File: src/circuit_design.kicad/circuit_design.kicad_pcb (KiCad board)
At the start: 2 copper layers, 220.3 x 182.9 mm, 184 parts, among them J1 CONN_BAT, Q1 BT136-600, Q2 BT136-600, Q3 BT136-600, Q4 BT136-600, U1 К176ИЕ12, U10 К155ЛА4, U11 К155ЛИ1, U12 К155ЛА1, U13 К155ИЕ5, U14 К155ЛЛ1, U15 К155ЛН1, U16 К155ЛИ1, U17 К155ТВ15, U18 К155ИЕ5, U19 К155ЛП5, U2 К155ЛП10, U20 К155ИВ1, U21 К155ИД7, U22 К155ИД4, U23 К155ЛН1, U24 К155ЛП10, U25 MOC3062M, U26 MOC3062M, U27 MOC3062M, U28 MOC3062M, U29 LM7806_TO220, U3 К155ЛЕ3, U30 SC6038, U31 К155ЛЕ1, U32 К155ЛН1, U33 К155ЛИ1, U34 К155ЛА4, U35 К155ТВ15, U36 К155ТЛ2, U37 4020, U38 LM7806_TO220, U39 К155ЛН1, U4 К155ЛН1, U5 К155ЛИ1, U6 К155ЛЛ1, U7 4020, U8 ICL7660, U9 К155ИЕ5, Y1 32768

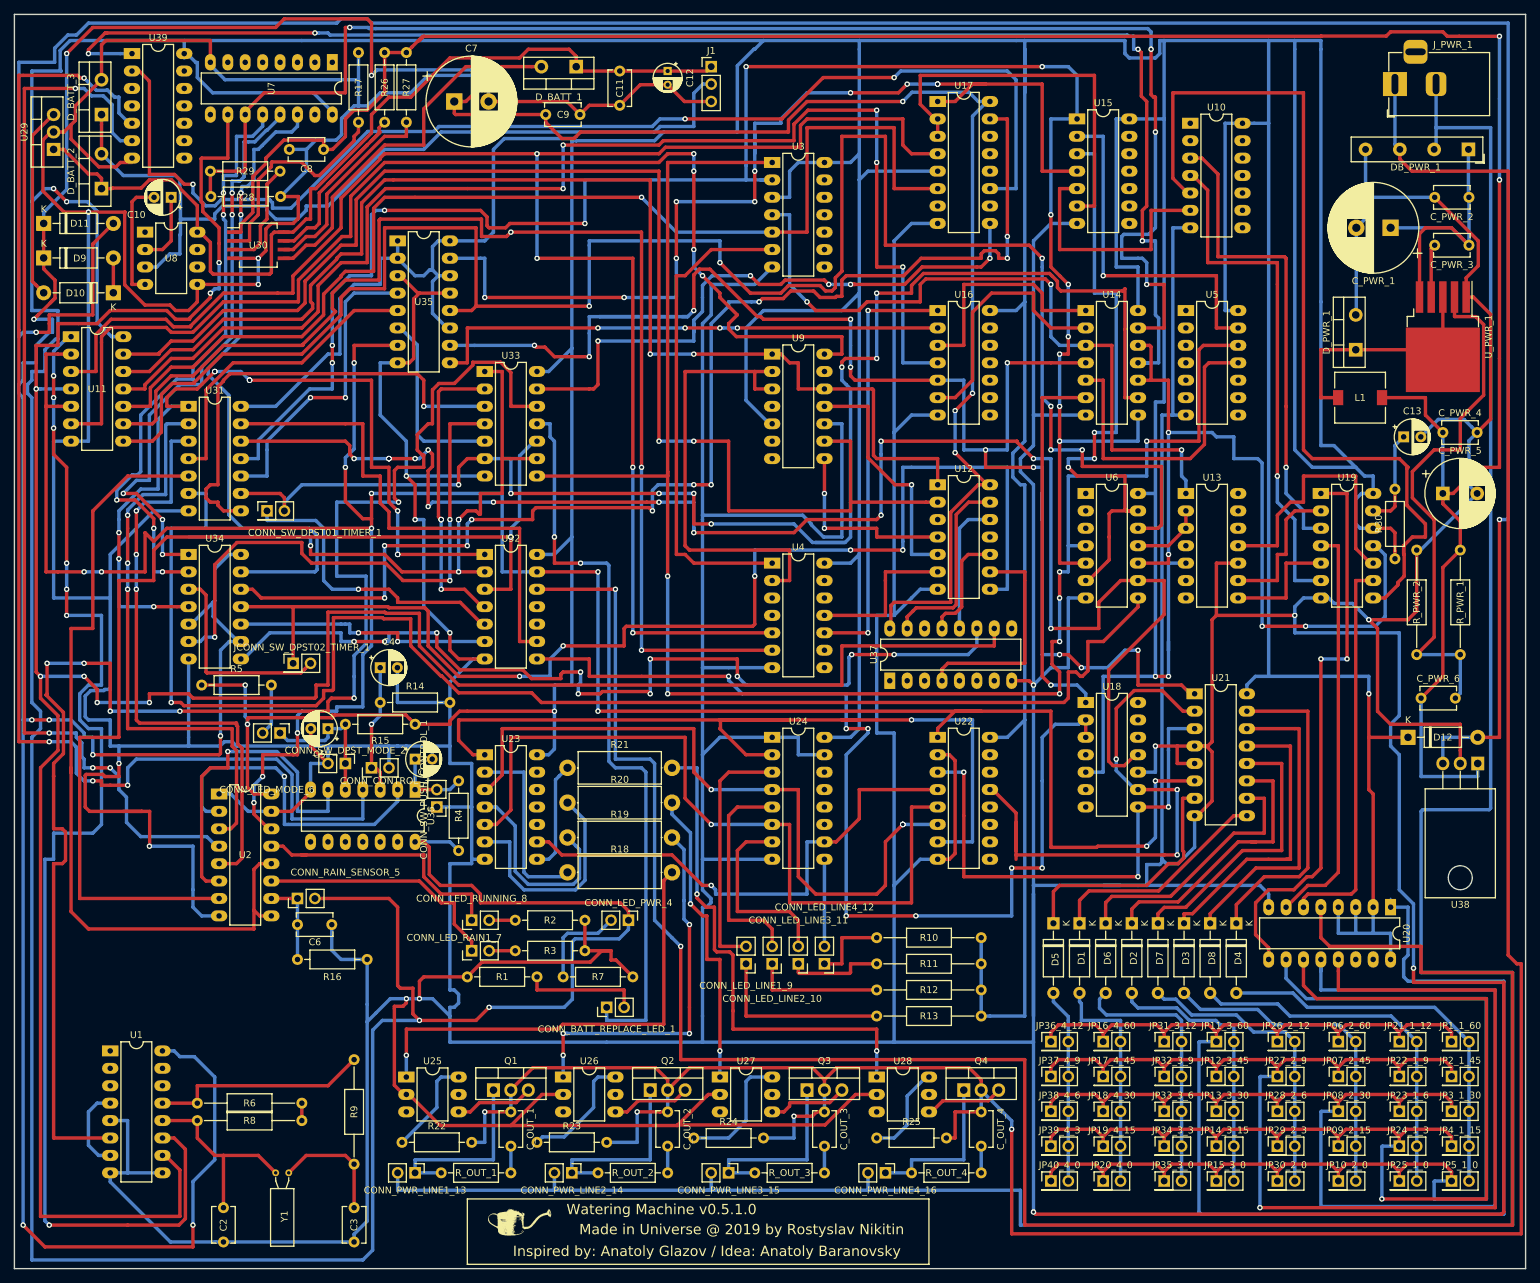
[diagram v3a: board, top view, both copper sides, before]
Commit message: 01. The BT136-600E triacs was replaced with the BT134-600E ones 02. The SMD drossel (L=47uH/0.88A) was replaced with the (L=47uH/2.5A) one 03. The board dimensions was decreased:     - Width:  220.345 -> 205.740 = 14.605     - Height: 182.880 -> 170.815 = 12.065
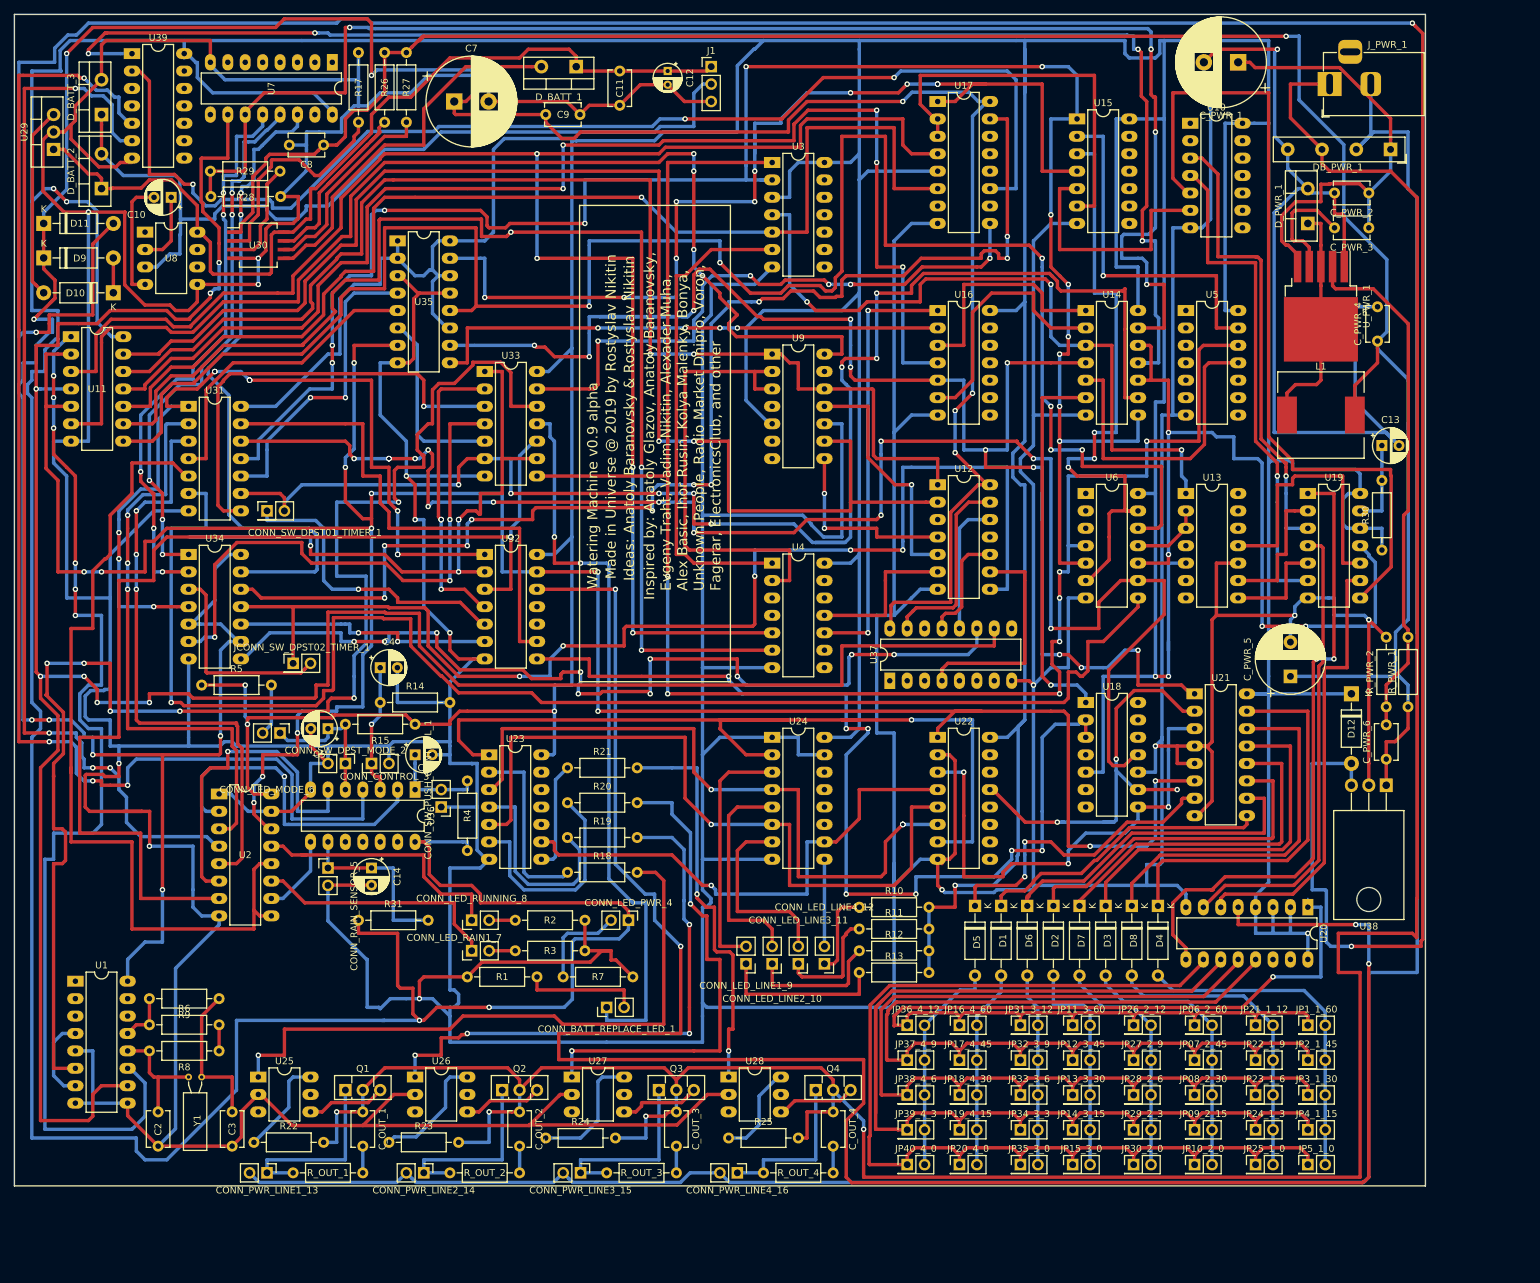
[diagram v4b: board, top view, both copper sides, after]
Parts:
- removed C6: 474, Capacitor_THT:C_Disc_D5.1mm_W3.2mm_P5.00mm
- removed G***: LOGO, logo:logo
- removed R16: 1KOhm, Resistor_THT:R_Axial_DIN0207_L6.3mm_D2.5mm_P10.16mm_Horizontal
- added C14: 100uF, Capacitor_THT:CP_Radial_D5.0mm_P2.50mm, F.Cu at (95.2, 133.3)
- added R31: 1KOhm, Resistor_THT:R_Axial_DIN0207_L6.3mm_D2.5mm_P10.16mm_Horizontal, F.Cu at (93.3, 141.0)
- L1: footprint Inductor_SMD:L_7.3x7.3_H4.5 -> Inductor_SMD:L_12x12mm_H6mm
- Q1, Q2, Q3, Q4: value BT136-600 -> BT134-600E; footprint Package_TO_SOT_THT:TO-220-3_Vertical -> Package_TO_SOT_THT:TO-126-3_Vertical
- R10, R11, R12, R13, R6, R8, R9, R_PWR_1, R_PWR_2: footprint Resistor_THT:R_Axial_DIN0207_L6.3mm_D2.5mm_P15.24mm_Horizontal -> Resistor_THT:R_Axial_DIN0207_L6.3mm_D2.5mm_P10.16mm_Horizontal
- R18, R19, R20, R21: footprint Resistor_THT:R_Axial_DIN0414_L11.9mm_D4.5mm_P15.24mm_Horizontal -> Resistor_THT:R_Axial_DIN0207_L6.3mm_D2.5mm_P10.16mm_Horizontal
- moved C_PWR_5 34.7 mm to (229.2, 105.4), turned to 90 degrees
- moved C_PWR_1 32.8 mm to (221.6, 15.9)
- moved R9 31.1 mm to (73.0, 152.4), turned to 180 degrees
- moved R_PWR_1 24.1 mm to (246.4, 109.9), turned to 90 degrees
- moved C3 22.6 mm to (74.9, 168.9)
- moved U27 21.6 mm to (124.5, 163.8)
- moved CONN_PWR_LINE4_16 21.6 mm to (148.6, 177.8)
- moved C_OUT_2 21.6 mm to (116.8, 168.9)
- moved C_OUT_3 21.6 mm to (139.7, 168.9)
- moved C_OUT_4 21.6 mm to (162.6, 168.9)
- moved Q1 21.6 mm to (91.4, 165.7)
- moved Q3 21.6 mm to (137.2, 165.7)
- moved Q4 21.6 mm to (160.0, 165.7)
- moved R24 21.6 mm to (120.7, 172.7)
- moved R25 21.6 mm to (147.3, 172.7)
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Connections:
- net Net-(C1-Pad1) renamed /Conn_Push_Control_Raw
- net Net-(C4-Pad1) renamed /Conn_Control_Raw
- net Net-(C5-Pad1) renamed /Mode_Raw
- CONN_RAIN_SENSOR_5 pad 1: /Rain_Sensor(Ext.) -> /Rain_Sensor_Raw
- CONN_RAIN_SENSOR_5 pad 2: +5V -> GND
- U36 pad 8: (no net) -> /Rain_Sensor(Ext.)
- U36 pad 9: (no net) -> /Rain_Sensor_Raw
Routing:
- net GND: track 2211.6 -> 1957.1 mm, vias 16 -> 15
- net +5V: track 1871.6 -> 1679.3 mm, vias 10 -> 11
- net PWR_ALW: track 579.2 -> 481.9 mm, vias 14 -> 13
- net /D4: track 210.6 -> 153.4 mm, vias 0 -> 1
- net Net-(D11-Pad2): track 406.9 -> 461.8 mm, vias 2 -> 3
- net /D3: track 190.6 -> 142.8 mm, vias 1 -> 0
- net /D2: track 180.6 -> 147.2 mm
- net GNDREF: track 379.3 -> 346.5 mm
- net +9V: track 357.8 -> 327.6 mm, vias 2 -> 1
- net CLK_MIN: track 399.7 -> 372.3 mm
- net Net-(R20-Pad2): track 44.4 -> 71.1 mm
- net Net-(R19-Pad2): track 55.7 -> 81.9 mm
- net /Rain_Sensor_Raw: track 0.00 -> 26.0 mm
- net Net-(U1-Pad11): track 183.7 -> 158.0 mm, vias 7 -> 6
- net Net-(R18-Pad2): track 67.5 -> 92.7 mm
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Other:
- board size 220.3 x 182.9 mm -> 205.7 x 170.8 mm
- board text added: "Ideas: Anatoly Baranovsky & Rostyslav Nikitin"
- board text added: "Inspired by: Anatoly Glazov, Anatoly Baranovsky, Evgeny Traht, Vadim Nikitin, Alexader Muha, Alex Basic, Ihor Rusin, Kolya Malenky, Bonya, Unknown People, Radio Market Dnipro, Voron, Fagerar, ElectronicsClub, and other"
- board text added: "Watering Machine v0.9 alpha"
- board text removed: "Inspired by: Anatoly Glazov / Idea: Anatoly Baranovsky"
- board text removed: "Watering Machine v0.5.1.0"

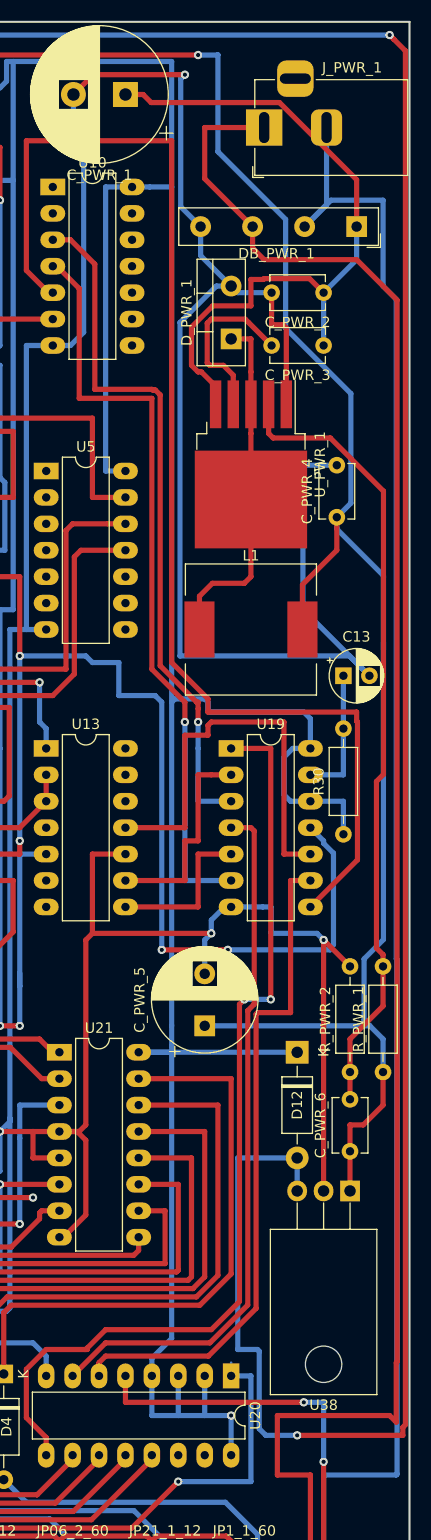
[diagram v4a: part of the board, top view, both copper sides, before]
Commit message: The PCB layout was optimized
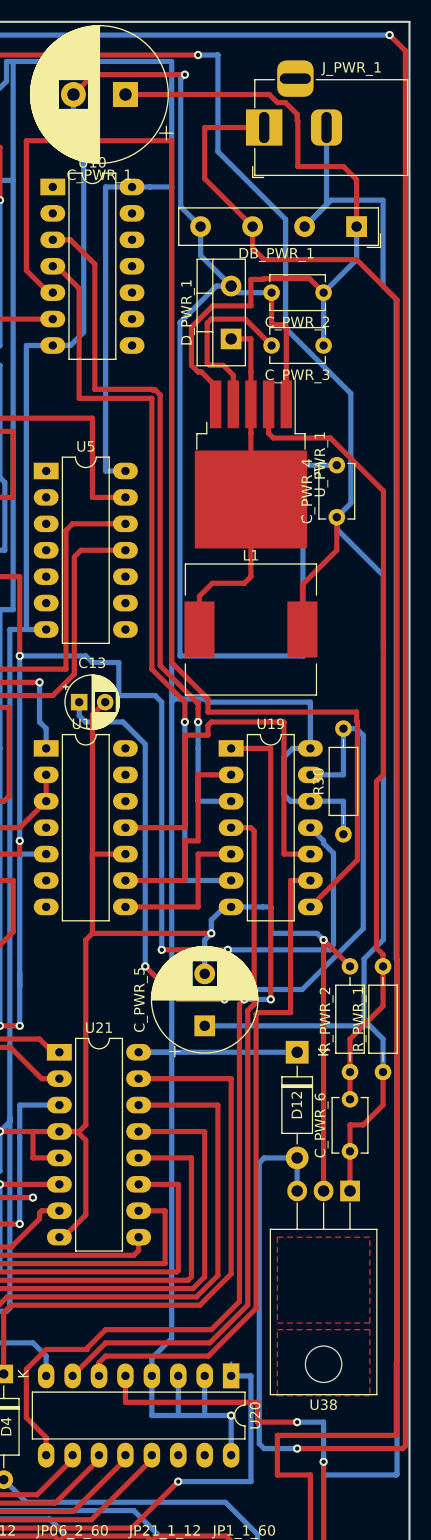
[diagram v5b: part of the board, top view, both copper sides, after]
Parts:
- moved C13 25.5 mm to (217.2, 74.3)
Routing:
- net Net-(C13-Pad1): track 12.1 -> 83.6 mm, vias 0 -> 2
- net GND: track 1957.1 -> 1961.3 mm
- net Net-(C_PWR_1-Pad1): track 68.1 -> 71.1 mm
- net Net-(D11-Pad2): track 461.8 -> 460.1 mm
- net VAC: track 416.6 -> 415.7 mm
- added copper zone on F.Cu, net (none)
